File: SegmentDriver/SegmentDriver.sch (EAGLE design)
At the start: 68 parts, among them K1 M02-MOLEX-104188-0210, K2 M02-MOLEX-104188-0210, K3 M02-MOLEX-104188-0210, K4 M02-MOLEX-104188-0210, K5 M02-MOLEX-104188-0210, K6 M02-MOLEX-104188-0210, K7 M02-MOLEX-104188-0210, K8 M02-MOLEX-104188-0210, K9 M02-MOLEX-104188-0210, Q1 MOSFET-NCHANNEL-FDMS5672, Q2 MOSFET-NCHANNEL-FDMS5672, Q3 MOSFET-NCHANNEL-FDMS5672, Q4 MOSFET-NCHANNEL-FDMS5672, Q5 MOSFET-NCHANNEL-FDMS5672, Q6 MOSFET-NCHANNEL-FDMS5672, Q7 MOSFET-NCHANNEL-FDMS5672, Q8 MOSFET-NCHANNEL-FDMS5672, Q9 MOSFET-NCHANNEL-FDMS5672, U1 FOD8321, U10 FOD8321, U13 DS1307SO8-TIGHT, U2 FOD8321, U3 FOD8321, U5 FOD8321, U6 FOD8321, U7 FOD8321, U8 FOD8321, U9 FOD8321, X1 32.768kHz

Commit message: Implemented RTD and RS485
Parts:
- removed K3, K5, K6, K7, K8, K9: M02-MOLEX-104188-0210, simbits:M02-MOLEX-104188-0210
- removed TP107: TEST-POINT3, SparkFun-Passives:TEST-POINT3
- added C11, C13, C15, C17, C18, C25: 47UF, Panasonic-EEEFK_EEEFP:EEE-FK1J470P-CASE-F
- added C12, C14, C16: 0.1uF, rcl:C-EUC1206K
- added C26, C27, C28, C29, C30, C33, C35, C36, C38, C39, C40, C41, C42, C43, C44, C45, C46, C47, C48, C49, C50, C51, C52, C53, C54, C55, C56, C57, C58, C59, C61, C62, C63, C64, C65, C66, C67, C68, C69, C70, C71, C73, C77, C78: 0.1uF, rcl:C-EUC0603K
- added C31, C32: 12pF, rcl:C-EUC0603K
- added C34, C37, C60: 1uF, rcl:C-EUC0603K
- added C72, C74, C75, C76: 220UF, Panasonic-EEEFK_EEEFP:EEE-FP1V221AP-CASE-F
- added H1, H2, H3, H4: MOUNT-PAD-ROUND3.0, simbits:MOUNT-PAD-ROUND3.0
- added IC2: ATMEGA644A, atmel:ATMEGA644A
- added K17: 61200621621, Wire-to-Board:61200621621
- added K18: 61201021621, Wire-to-Board:61201021621
- added KD1, KD2, KS1, KS2, KS3, KS4, KS5, KS6, KS7: M02-MOLEX-104188-0210, simbits:M02-MOLEX-104188-0210
- added KT1, KT2, KT3, KT4, KT5, KT6, KT7, KTD1, KTD2: 691321100004, Wurth_Elektronik_Electromechanic_Terminal_Blocks_Connectors_rev15d:691321100004
- added LED1, LED2: (no value), led:LED5MM
- added LED5, LED6: (no value), adafruit:LEDCHIPLED_0603
- added LED7, LED8: AMBER, adafruit:LEDCHIPLED_0603
- added Q10, Q11: (no value), simbits:DMG1012T
- added R18, R31, R35, R53, R54: 1k, rcl:R-EU_R0603
- added R19, R20, R21, R22, R23, R24, R25, R26, R27, R29, R30, R34, R36: 0R, rcl:R-EU_R0603
- added R28: 10k, rcl:R-EU_R0603
- added R32, R33: 4.7k, rcl:R-EU_R0603
- added R37, R38, R39, R40, R41, R42, R43, R44, R45, R46: 100k, rcl:R-EU_R0603
- added R47: 1.2K, rcl:R-EU_R0603
- added R48: 2K4, rcl:R-EU_R0603
- added RESET_SW: SPST_TACT-EVQQ2, adafruit:SPST_TACT-EVQQ2
- added U14: (no value), simbits:ADS1X48IPW
- added Y1: (no value), SparkFun-FreqCtrl:CRYSTAL5X3
- C19, C20, C23: value 1uF -> 0.1uF
- C3, C4, C6: value 0.1uF -> 47UF; device rcl:C-EUC1206K -> Panasonic-EEEFK_EEEFP:EEE-FK1J470P-CASE-F
- K1, K2: value M02-MOLEX-104188-0210 -> 691318500002; device simbits:M02-MOLEX-104188-0210 -> TerminalBlocks:691318500002
- K4: value M02-MOLEX-104188-0210 -> 691321100005; device simbits:M02-MOLEX-104188-0210 -> Wurth_Elektronik_Electromechanic_Terminal_Blocks_Connectors_rev15d:691321100005
- R11: value 330R -> 100k
- R12: value 1K21 -> 100k
- R13: value 205R -> 0R
- R14, R16: value 330R -> 0R
- R15, R17: value 1K21 -> 0R
- U15: device simbits:ADS1X48IPW -> LINE_DRIVERS:ISL83078E
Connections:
- removed net N$14 (its old number): K4.1, Q4.D
- removed net N$16 (its old number): K6.1, Q6.D
- removed net N$7 (its old number): K3.1, Q3.D
- removed net T5: C22.1, R11.2, R15.2
- removed net T6: C24.1, R16.2, R17.2
- removed net TREF: C20.1, R14.1
- new net !INT_PROJECTOR: IC2.(PCINT27/INT1)PD3
- new net !RESET: IC2.RESET, K17.5, K18.6, R28.1, RESET_SW.P, RESET_SW.P1
- new net AD1_!CS: U11.!CS!@24
- new net AD1_!DRDY: U11.!DRDY!@25
- new net AD1_!RESET: R11.1, U11.!RESET!@4
- new net AD1_AIN0: KT1.4, U11.AIN0/IEXC@11
- new net AD1_AIN1: C19.2, C20.1, R13.1, U11.AIN1/IEXC@12
- new net AD1_AIN2: C19.1, C22.2, R14.1, U11.AIN2/IEXC/GPIO2@17
- new net AD1_AIN3: KT2.4, U11.AIN3/IEXC/GPIO3@18
- new net AD1_AIN4: C23.2, C24.1, R15.1, U11.AIN4/IEXC/GPIO4@13
- new net AD1_AIN5: C23.1, C38.2, R16.1, U11.AIN5/IEXC/GPIO5@14
- new net AD1_AIN6: C39.2, C40.1, R17.1, U11.AIN6/IEXC/GPIO6@15
- new net AD1_AIN7: C39.1, C41.2, R19.1, U11.AIN7/IEXC/GPIO7@16
- new net AD1_BIASP: KT1.1, KT2.1, KT3.1, R38.2, R39.1
- new net AD1_IEXC1: KT3.4
- new net AD1_START: U11.START@23
- new net AD2_!CS: U12.!CS!@24
- new net AD2_!DRDY: U12.!DRDY!@25
- new net AD2_!RESET: R12.1, U12.!RESET!@4
- new net AD2_AIN0: KT4.4, U12.AIN0/IEXC@11
- new net AD2_AIN1: C42.2, C43.1, R20.1, U12.AIN1/IEXC@12
- new net AD2_AIN2: C42.1, C44.2, R21.1, U12.AIN2/IEXC/GPIO2@17
- new net AD2_AIN3: KT5.4, U12.AIN3/IEXC/GPIO3@18
- new net AD2_AIN4: C45.2, C46.1, R22.1, U12.AIN4/IEXC/GPIO4@13
- new net AD2_AIN5: C45.1, C47.2, R23.1, U12.AIN5/IEXC/GPIO5@14
- new net AD2_AIN6: C48.2, C49.1, R24.1, U12.AIN6/IEXC/GPIO6@15
- new net AD2_AIN7: C48.1, C50.2, R25.1, U12.AIN7/IEXC/GPIO7@16
- new net AD2_BIASP: KT4.1, KT5.1, KT6.1, R41.2, R42.1, R44.2, R45.1
- new net AD2_IEXC1: KT6.4
- new net AD2_START: U12.START@23
- new net AD3_!CS: U14.!CS!@24
- new net AD3_!DRDY: U14.!DRDY!@25
- new net AD3_!RESET: R37.1, U14.!RESET!@4
- new net AD3_AIN0: KT7.4, U14.AIN0/IEXC@11
- new net AD3_AIN1: C51.2, C52.1, R26.1, U14.AIN1/IEXC@12
- new net AD3_AIN2: C51.1, C53.2, R27.1, U14.AIN2/IEXC/GPIO2@17
- new net AD3_AIN3: KTD1.4, U14.AIN3/IEXC/GPIO3@18
- new net AD3_AIN4: C54.2, C55.1, R29.1, U14.AIN4/IEXC/GPIO4@13
- new net AD3_AIN5: C54.1, C56.2, R30.1, U14.AIN5/IEXC/GPIO5@14
- new net AD3_AIN6: C57.2, C58.1, R34.1, U14.AIN6/IEXC/GPIO6@15
- new net AD3_AIN7: C57.1, C59.2, R36.1, U14.AIN7/IEXC/GPIO7@16
- new net AD3_BIASP: KT7.1, KTD1.1, KTD2.1
- new net AD3_IEXC1: KTD2.4
- new net AD3_START: U14.START@23
- new net AVDD: C33.1, C36.1, C62.1, U11.AVDD@22, U12.AVDD@22, U14.AVDD@22
- new net CS_ADS1248_1: IC2.(PCINT2/ADC2)PA2
- new net CS_ADS1248_2: IC2.(PCINT1/ADC1)PA1
- new net CS_ADS1248_3: IC2.(PCINT0/ADC0)PA0
- new net DVDD: C21.1, C35.1, C61.1, R11.2, R12.2, R37.2, U11.DVDD@1, U12.DVDD@1, U14.DVDD@1
- new net LED1: IC2.(PCINT7/ADC7)PA7, R35.1
- new net LED2: IC2.(PCINT6/ADC6)PA6, R31.1
- new net MISO: IC2.(PCINT14/MISO)PB6, K17.1, U11.DOUT/!DRDY!@26, U12.DOUT/!DRDY!@26, U14.DOUT/!DRDY!@26
- new net MOSI: IC2.(PCINT13/MOSI)PB5, K17.4, U11.DIN@27, U12.DIN@27, U14.DIN@27
- new net N$11: C11.1, KS4.1, Q4.D
- new net N$13: C13.1, KS5.1, Q5.D
- new net N$25: LED7.C, R53.2
- new net N$26: LED8.C, R54.2
- new net N$27: KT1.2, R14.2
- new net N$28: KT3.3, R17.2
- new net N$29: C29.2, IC2.AREF
- new net N$30: C34.1, U11.VREFOUT@9
- new net N$31: KT3.2, R19.2
- new net N$32: LED5.A, R31.2
- new net N$33: LED6.A, R35.2
- new net N$34: KT4.3, R20.2
- new net N$35: KT4.2, R21.2
- new net N$36: IC2.(PCINT23/TOSC2)PC7
- new net N$37: IC2.(PCINT22/TOSC1)PC6
- new net N$38: IC2.(PCINT31/OC2A)PD7
- new net N$39: C32.1, IC2.XTAL1, Y1.1
- new net N$40: C31.1, IC2.XTAL2, Y1.2
- new net N$41: C37.1, U12.VREFOUT@9
- new net N$42: KT5.3, R22.2
- new net N$43: KT5.2, R23.2
- new net N$44: KT6.3, R24.2
- new net N$45: KT6.2, R25.2
- new net N$46: KT7.3, R26.2
- new net N$47: IC2.(PCINT24/RXD0)PD0, R18.2
- new net N$48: KT7.2, R27.2
- new net N$49: KTD1.3, R29.2
- new net N$50: KTD1.2, R30.2
- new net N$51: KTD2.3, R34.2
- new net N$52: KTD2.2, R36.2
- new net N$53: C60.1, U14.VREFOUT@9
- new net N$54: C67.2, C68.1, R43.2, U12.REFN0/GPIO1@6
- new net N$55: C64.2, C65.1, R40.2, U11.REFN0/GPIO1@6
- new net N$56: C66.2, C67.1, R42.2, U12.REFP0/GPIO0@5
- new net N$57: C63.2, C64.1, R39.2, U11.REFP0/GPIO0@5
- new net N$58: C70.2, C71.1, R46.2, U14.REFN0/GPIO1@6
- new net N$59: C69.2, C70.1, R45.2, U14.REFP0/GPIO0@5
- new net N$60: Q11.D, R54.1
- new net N$61: Q10.D, R53.1
- new net N$62: LED2.A, R47.1
- new net N$63: LED1.A, R48.1
- new net N$64: U15.RE
- new net N$8: C6.1, KS3.1, Q3.D
- new net POWERFAIL: IC2.(PCINT30/OC2B/ICP)PD6
- new net POWERGOOD: IC2.(PCINT29/OC1A)PD5
- new net PWRON: IC2.(PCINT28/OC1B)PD4
- new net RS485+: K4.1, K4.3, U15.A/Y
- new net RS485-: K4.2, K4.4, U15.B/Z
- new net SCK: IC2.(PCINT15/SCK)PB7, K17.3, U11.SCLK@28, U12.SCLK@28, U14.SCLK@28
- new net TCK: IC2.(PCINT18/TCK)PC2, K18.1
- new net TDI: IC2.(PCINT21/TDI)PC5, K18.9
- new net TDO: IC2.(PCINT20/TDO)PC4, K18.3
- new net TMS: IC2.(PCINT19/TMS)PC3, K18.5
- new net UART_DE: IC2.(PCINT5/ADC5)PA5, U15.DE
- new net UART_RX: Q10.G, R18.1, U15.R0
- new net UART_TX: IC2.(PCINT25/TXD0)PD1, Q11.G, U15.DI
- net +12V: now also C12.1, C14.1, C16.1, C74.1, C75.1, C77.2, K2.2, R47.2; no longer C3.1, C4.1, C6.1
- net +24V: now also C72.1, C76.1, C78.2, KD1.2, KD2.2, KS1.2, KS2.2, KS3.2, KS4.2, KS5.2, KS6.2, KS7.2, R48.2; no longer K2.2, K3.2, K4.2, K5.2, K6.2, K7.2, K8.2, K9.2
- net 3.3V: now also C73.1, LED7.A, LED8.A, U15.VCC; no longer R12.1, R15.1, R17.1
- net 5V: now also C26.2, C27.2, C28.2, C30.2, IC2.AVCC, IC2.VCC, IC2.VCC@1, IC2.VCC@2, K17.2, K18.4, R28.2, R32.2, R33.2
- net AGND: now also C11.2, C13.2, C15.2, C17.2, C18.2, C25.2, C3.2, C4.2, C6.2
- net GND: now also C12.2, C14.2, C16.2, C22.1, C26.1, C27.1, C28.1, C29.1, C30.1, C31.2, C32.2, C33.2, C34.2, C35.2, C36.2, C37.2, C38.1, C40.2, C41.1, C43.2, C44.1, C46.2, C47.1, C49.2, C50.1, C52.2, C53.1, C55.2, C56.1, C58.2, C59.1, C60.2, C61.2, C62.2, C63.1, C65.2, C66.1, C68.2, C69.1, C71.2, C72.2, C73.2, C74.2, C75.2, C76.2, C77.1, C78.1, H1.MOUNT, H2.MOUNT, H3.MOUNT, H4.MOUNT, IC2.GND, IC2.GND@1, IC2.GND@2, IC2.GND@3, K1.1, K17.6, K18.10, K18.2, K2.1, LED1.C, LED2.C, LED5.C, LED6.C, Q10.S, Q11.S, R38.1, R40.1, R41.1, R43.1, R44.1, R46.1, RESET_SW.S, RESET_SW.S1, U11.AVSS@21, U11.CLK@3, U11.DGND@2, U11.VREFCOM@10, U12.AVSS@21, U12.CLK@3, U12.DGND@2, U12.VREFCOM@10, U14.AVSS@21, U14.CLK@3, U14.DGND@2, U14.VREFCOM@10, U15.GND; no longer C19.2, C22.2, C23.2, C3.2, C4.2, C6.2, R13.2, U15.DIN@27
- net IIC1_SCL: now also IC2.(PCINT16/SCL)PC0, R32.1
- net IIC1_SDA: now also IC2.(PCINT17/SDA)PC1, R33.1
- net N$15: now also C15.1, KS6.1, Q6.D; no longer K5.1, Q5.D
- net N$17: now also C17.1, KS7.1; no longer K7.1
- net N$18: now also C18.1, KD1.1; no longer K9.1
- net N$19: now also C25.1, KD2.1; no longer K8.1
- net N$20: now also KT2.3, R15.2; no longer C19.1, R11.1
- net N$22: now also KT2.2, R16.2; no longer R12.2, R13.1, R14.2, TP107.1
- net N$23: now also KT1.3, R13.2; no longer C23.1, R16.1
- net N$3: now also C3.1, KS1.1; no longer K1.1
- net N$6: now also C4.1, KS2.1; no longer K2.1
- net PWM_DOT1: now also R9.1; no longer R8.1
- net PWM_DOT2: now also R8.1; no longer R9.1
- net RTC_1HZ_CLK: now also IC2.(PCINT26/INT0)PD2
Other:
- note added: "PWR 12V"
- note added: "PWR 24V"

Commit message: Added ext. gpio, 7 seg. driver, differential filtering
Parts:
- removed K4: 691321100005, Wurth_Elektronik_Electromechanic_Terminal_Blocks_Connectors_rev15d:691321100005
- removed LED2: (no value), led:LED5MM
- added C79, C80: 0.1uF, rcl:C-EUC0603K
- added IC1: PCA9555PW, micro-philips:PCA9555PW
- added IC3: 4511D, 45xx:4511D
- added K3: (no value), Wurth_Elektronik_Electromechanic_Input-Output_Connectors_rev15c:615016149521
- added KB1, KB2, KB3, KB4, KB5, KB6: 53261-03, con-molex:53261-03
- added R49, R50, R51, R52, R55, R69: 33R, simbits:EXBV8V330JV
- added R56, R57, R59: 47R, simbits:EXBV8V330JV
- added R58: 10k, rcl:R-EU_R0603
- added R60: 1k, simbits:EXBV8V330JV
- C11, C13, C15, C17, C18, C25, C3, C4, C6: value 47UF -> 470UF; device Panasonic-EEEFK_EEEFP:EEE-FK1J470P-CASE-F -> Panasonic-EEEFK_EEEFP:EEE-FK1J471AM-CASE-J16
- C72, C76: value 220UF -> 470UF; device Panasonic-EEEFK_EEEFP:EEE-FP1V221AP-CASE-F -> Panasonic-EEEFK_EEEFP:EEE-FK1J471AM-CASE-J16
- KT1, KT2, KT3, KT4, KT5, KT6, KT7, KTD1, KTD2: value 691321100004 -> 691210910004; device Wurth_Elektronik_Electromechanic_Terminal_Blocks_Connectors_rev15d:691321100004 -> Wurth_Elektronik_Electromechanic_Terminal_Blocks_Connectors_rev15d:691210910004
- LED1: value (none) -> 7-SEG_SA02-107; device led:LED5MM -> display-kingbright-2:7-SEG_SA02-107
- Q10, Q11: value (none) -> DMP2215L-7; device simbits:DMG1012T -> simbits:DMP2215L-7
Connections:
- removed net !INT_PROJECTOR: IC2.(PCINT27/INT1)PD3
- removed net 3.3V: C73.1, LED7.A, LED8.A, U15.VCC
- removed net POWERFAIL: IC2.(PCINT30/OC2B/ICP)PD6
- removed net POWERGOOD: IC2.(PCINT29/OC1A)PD5
- removed net PWRON: IC2.(PCINT28/OC1B)PD4
- new net EXTGPIO_!INT: IC1.!INT, IC2.(PCINT27/INT1)PD3, R58.1
- new net GPIO1: KB1-2.S, R56.8
- new net GPIO2: KB2-2.S, R56.7
- new net GPIO3: KB3-2.S, R56.6
- new net GPIO4: KB4-2.S, R56.5
- new net GPIO5: KB5-2.S, R57.8
- new net GPIO6: KB6-2.S, R57.7
- new net GPIO7: R57.6
- new net GPIO8: R57.5
- new net N$100: LED1.E, R60.8
- new net N$101: LED1.F, R60.7
- new net N$102: LED1.G, R60.6
- new net N$103: LED1.DP, R60.5
- new net N$104: IC1.I/O1.1, IC3A.IB
- new net N$105: IC1.I/O1.2, IC3A.IC
- new net N$106: IC1.I/O1.3, IC3A.ID
- new net N$107: IC1.I/O1.4, IC3A.LE
- new net N$108: IC1.I/O1.5, R60.4
- new net N$65: R49.5, U11.!DRDY!@25
- new net N$66: R69.8, U11.!CS!@24
- new net N$67: R69.7, U11.DIN@27
- new net N$68: R69.6, U11.DOUT/!DRDY!@26
- new net N$69: R69.5, U11.SCLK@28
- new net N$70: R49.8, U11.START@23
- new net N$71: R51.5, U14.SCLK@28
- new net N$72: R51.6, U14.DOUT/!DRDY!@26
- new net N$73: R51.7, U14.DIN@27
- new net N$74: R51.8, U14.!CS!@24
- new net N$75: R50.5, U14.!DRDY!@25
- new net N$76: R50.8, U14.START@23
- new net N$77: R52.5, U12.SCLK@28
- new net N$78: R52.6, U12.DOUT/!DRDY!@26
- new net N$79: R52.7, U12.DIN@27
- new net N$80: R52.8, U12.!CS!@24
- new net N$81: R55.5, U12.!DRDY!@25
- new net N$82: R55.8, U12.START@23
- new net N$83: IC1.I/O0.3, R56.4
- new net N$84: IC1.I/O0.4, R57.1
- new net N$85: IC1.I/O0.5, R57.2
- new net N$86: IC1.I/O0.6, R57.3
- new net N$87: IC1.I/O0.7, R57.4
- new net N$88: IC1.I/O1.0, IC3A.IA
- new net N$89: IC3A.A, R59.1
- new net N$90: IC3A.B, R59.2
- new net N$91: IC3A.C, R59.3
- new net N$92: IC3A.D, R59.4
- new net N$93: IC3A.E, R60.1
- new net N$94: IC3A.F, R60.2
- new net N$95: IC3A.G, R60.3
- new net N$96: LED1.A, R59.8
- new net N$97: LED1.B, R59.7
- new net N$98: LED1.C, R59.6
- new net N$99: LED1.D, R59.5
- net +5V: now also C73.1, C79.1, C80.1, IC1.VDD, IC3A.BI, IC3A.LT, IC3P.VDD, KB1-1.S, KB2-1.S, KB3-1.S, KB4-1.S, KB5-1.S, KB6-1.S, Q10.S, Q11.S, R58.2, U15.VCC
- net AD1_!CS: now also R69.1; no longer U11.!CS!@24
- net AD1_!DRDY: now also R49.4; no longer U11.!DRDY!@25
- net AD1_START: now also R49.1; no longer U11.START@23
- net AD2_!CS: now also R52.1; no longer U12.!CS!@24
- net AD2_!DRDY: now also R55.4; no longer U12.!DRDY!@25
- net AD2_START: now also R55.1; no longer U12.START@23
- net AD3_!CS: now also R51.1; no longer U14.!CS!@24
- net AD3_!DRDY: now also R50.4; no longer U14.!DRDY!@25
- net AD3_START: now also R50.1; no longer U14.START@23
- net GND: now also C79.2, C80.2, IC1.A0, IC1.A1, IC1.A2, IC1.VSS, IC3P.VSS, KB1-3.S, KB2-3.S, KB3-3.S, KB4-3.S, KB5-3.S, KB6-3.S, LED1.COM@1, LED1.COM@2, R53.1, R54.1; no longer LED1.C, LED2.C, Q10.S, Q11.S
- net IIC1_SCL: now also IC1.SCL
- net IIC1_SDA: now also IC1.SDA
- net MISO: now also R51.3, R52.3, R69.3; no longer U11.DOUT/!DRDY!@26, U12.DOUT/!DRDY!@26, U14.DOUT/!DRDY!@26
- net MOSI: now also R51.2, R52.2, R69.2; no longer U11.DIN@27, U12.DIN@27, U14.DIN@27
- net N$36: now also IC1.I/O0.0, R56.1; no longer IC2.(PCINT23/TOSC2)PC7
- net N$37: now also IC1.I/O0.1, R56.2; no longer IC2.(PCINT22/TOSC1)PC6
- net N$38: now also IC1.I/O0.2, R56.3; no longer IC2.(PCINT31/OC2A)PD7
- net N$60: now also LED7.A, Q10.D; no longer Q11.D, R54.1
- net N$61: now also LED8.A, Q11.D; no longer Q10.D, R53.1
- net N$62: no longer LED2.A
- net N$63: no longer LED1.A
- net RS485+: now also K3.A2, K3.B1; no longer K4.1, K4.3
- net RS485-: now also K3.A1, K3.B2; no longer K4.2, K4.4
- net SCK: now also R51.4, R52.4, R69.4; no longer U11.SCLK@28, U12.SCLK@28, U14.SCLK@28
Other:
- note added: "I2C Addr (7-bit): 0x21"

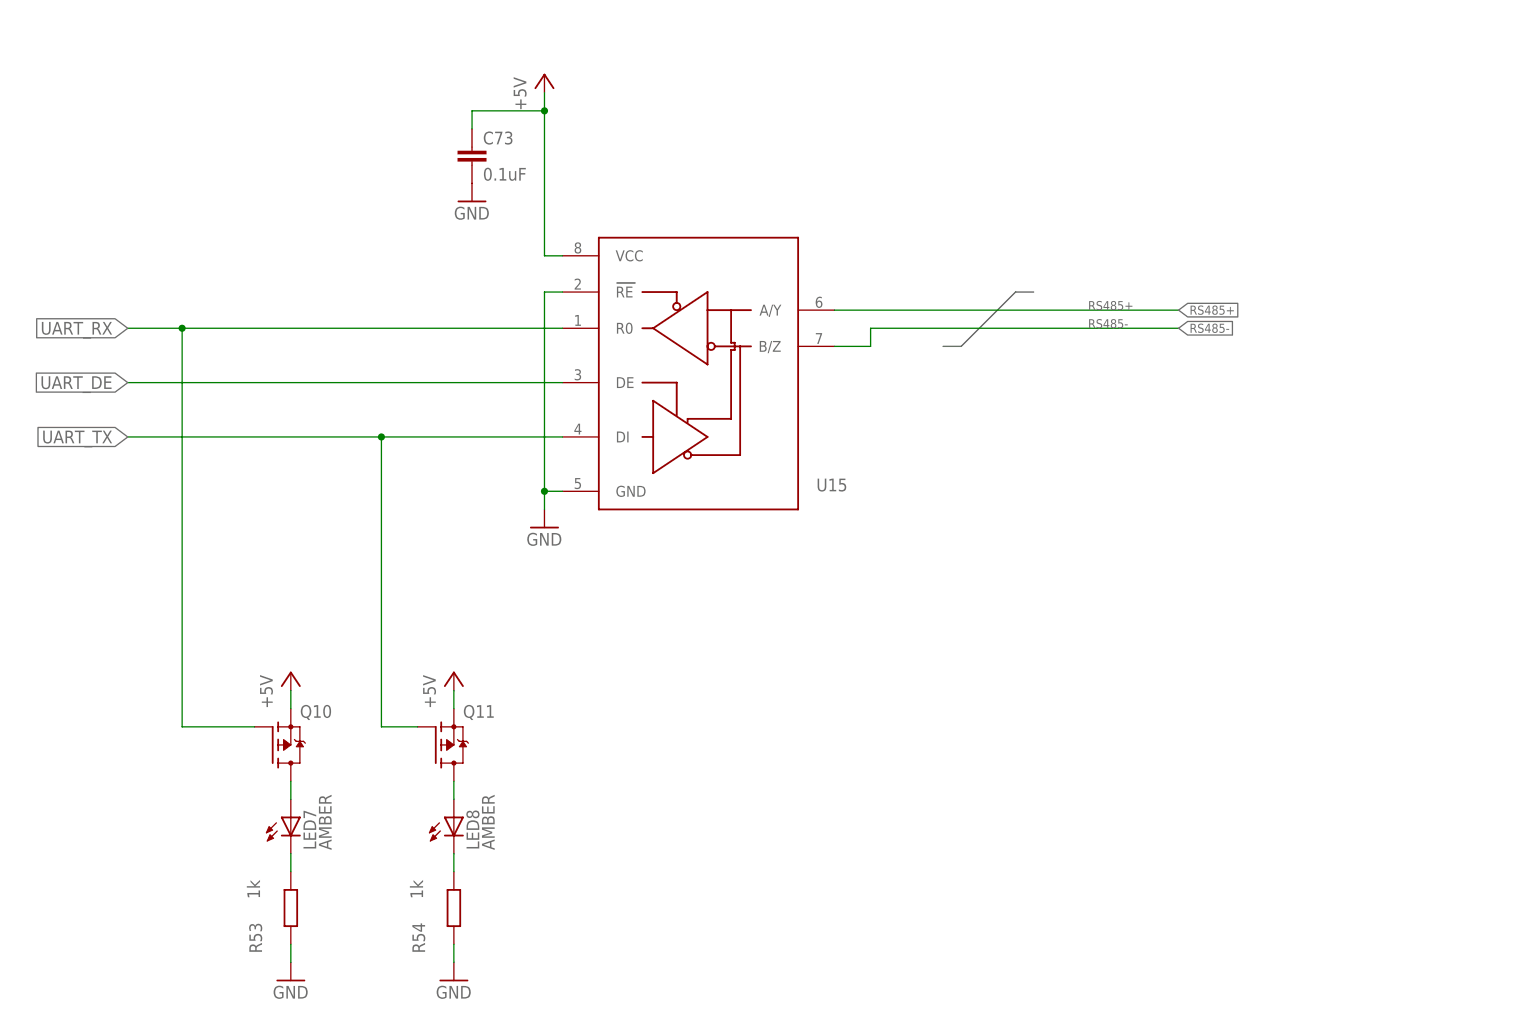
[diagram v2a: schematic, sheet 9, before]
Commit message: reduced size to 175mm
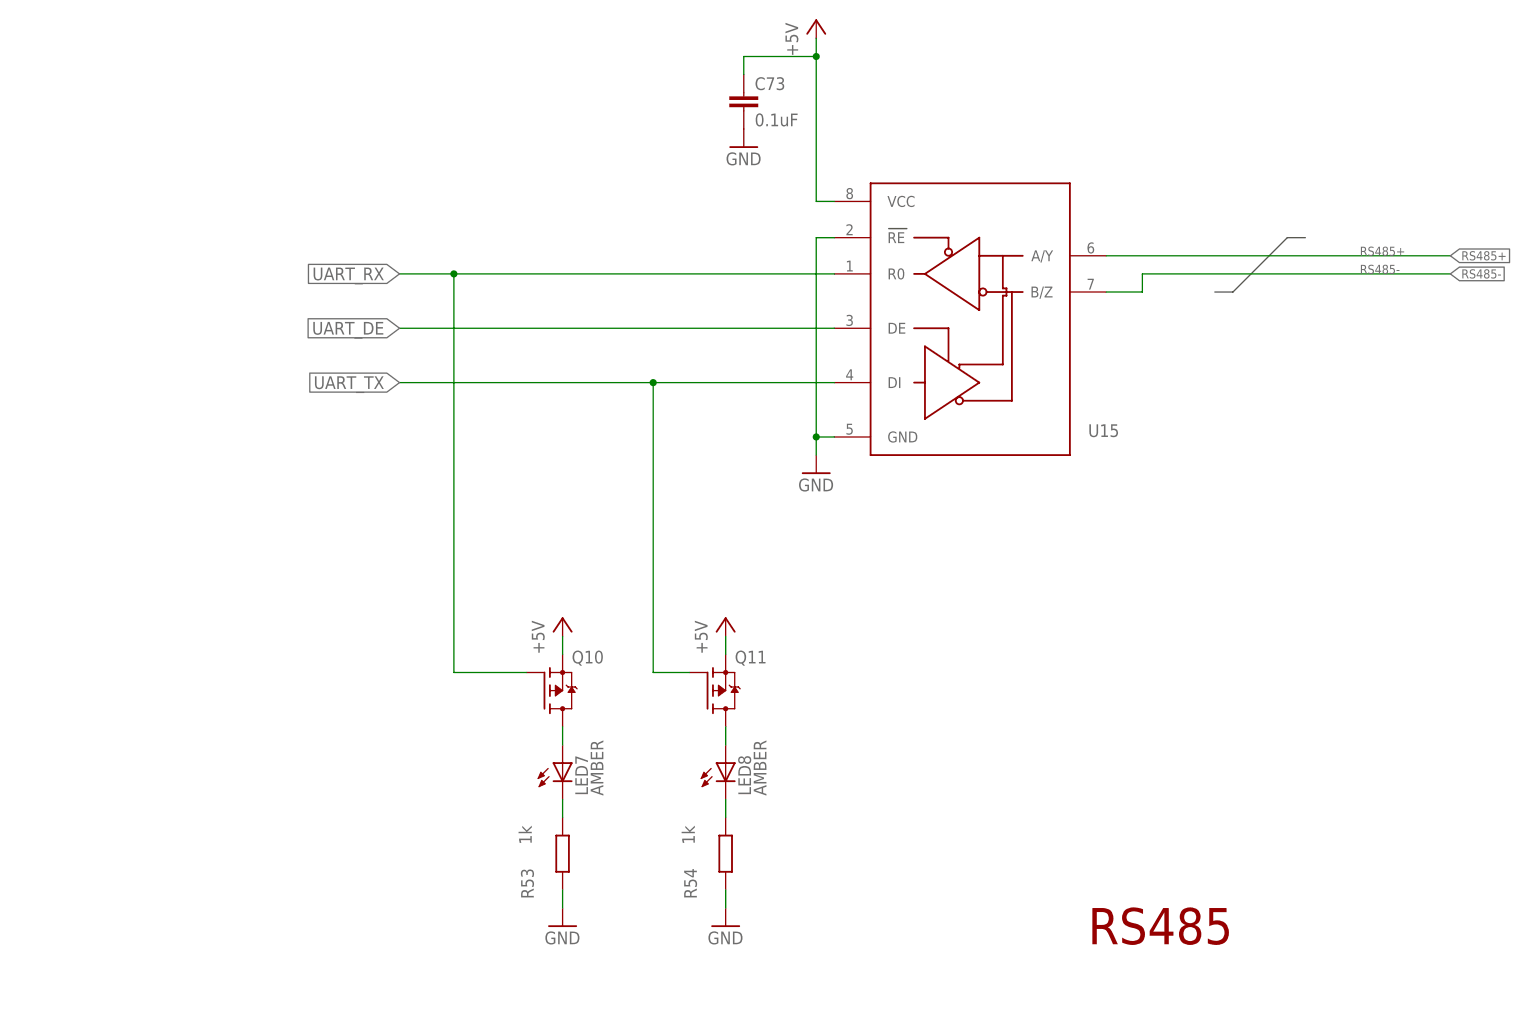
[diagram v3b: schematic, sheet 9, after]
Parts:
- added H5, H6, H7: MOUNT-HOLE2.0, simbits:MOUNT-HOLE2.0
- added H9: MOUNT-PAD-ROUND2,0, simbits:MOUNT-PAD-ROUND2,0
- added K4: 691313710002, Wurth_Elektronik_Electromechanic_Terminal_Blocks_Connectors_rev15d:691313710002
- added K5: 691322310002, Wurth_Elektronik_Electromechanic_Terminal_Blocks_Connectors_rev15d:691322310002
- added LED2, LED3: (no value), adafruit:LEDCHIPLED_0603
- C11, C13, C15, C17, C18, C25, C3, C4, C6: value 470UF -> 220UF; device Panasonic-EEEFK_EEEFP:EEE-FK1J471AM-CASE-J16 -> Panasonic-EEEFK_EEEFP:EEE-FK1J221AQ-CASE-H13
- H1, H2, H3, H4: value MOUNT-PAD-ROUND3.0 -> MOUNT-PAD-ROUND2,0; device simbits:MOUNT-PAD-ROUND3.0 -> simbits:MOUNT-PAD-ROUND2,0
- K1: value 691318500002 -> 691313710002; device TerminalBlocks:691318500002 -> Wurth_Elektronik_Electromechanic_Terminal_Blocks_Connectors_rev15d:691313710002
- K2: value 691318500002 -> 691322310002; device TerminalBlocks:691318500002 -> Wurth_Elektronik_Electromechanic_Terminal_Blocks_Connectors_rev15d:691322310002
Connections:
- net +12V: now also K2.1, K5.2; no longer K2.2
- net +24V: now also K1.1, K4.2; no longer K1.2
- net GND: now also H9.MOUNT, K1.2, K2.2, K4.1, K5.1, LED2.C, LED3.C; no longer K1.1, K2.1
- net N$62: now also LED3.A
- net N$63: now also LED2.A
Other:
- note added: "Ext GPIO & 7-Seg"
- note added: "Heater PWM"
- note added: "Heater output stage"
- note added: "I/O Connectors"
- note added: "MCU"
- note added: "Power in/out"
- note added: "RS485"
- note added: "RTC"
- note added: "RTD ADCs"
- note added: "RTD input filters"
- note removed: "PP-OUT schematic module"
- moved on the sheet: C73, K1, K2, LED7, LED8, Q10, Q11, R53, R54, U15
